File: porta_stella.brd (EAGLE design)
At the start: 220 x 100 mm, 85 parts, among them IC1 74LS00D, T1 2N3904, T2 PN3906, T3 PN3906, T4 PN3906, X1 SSW-112-02-G-Q

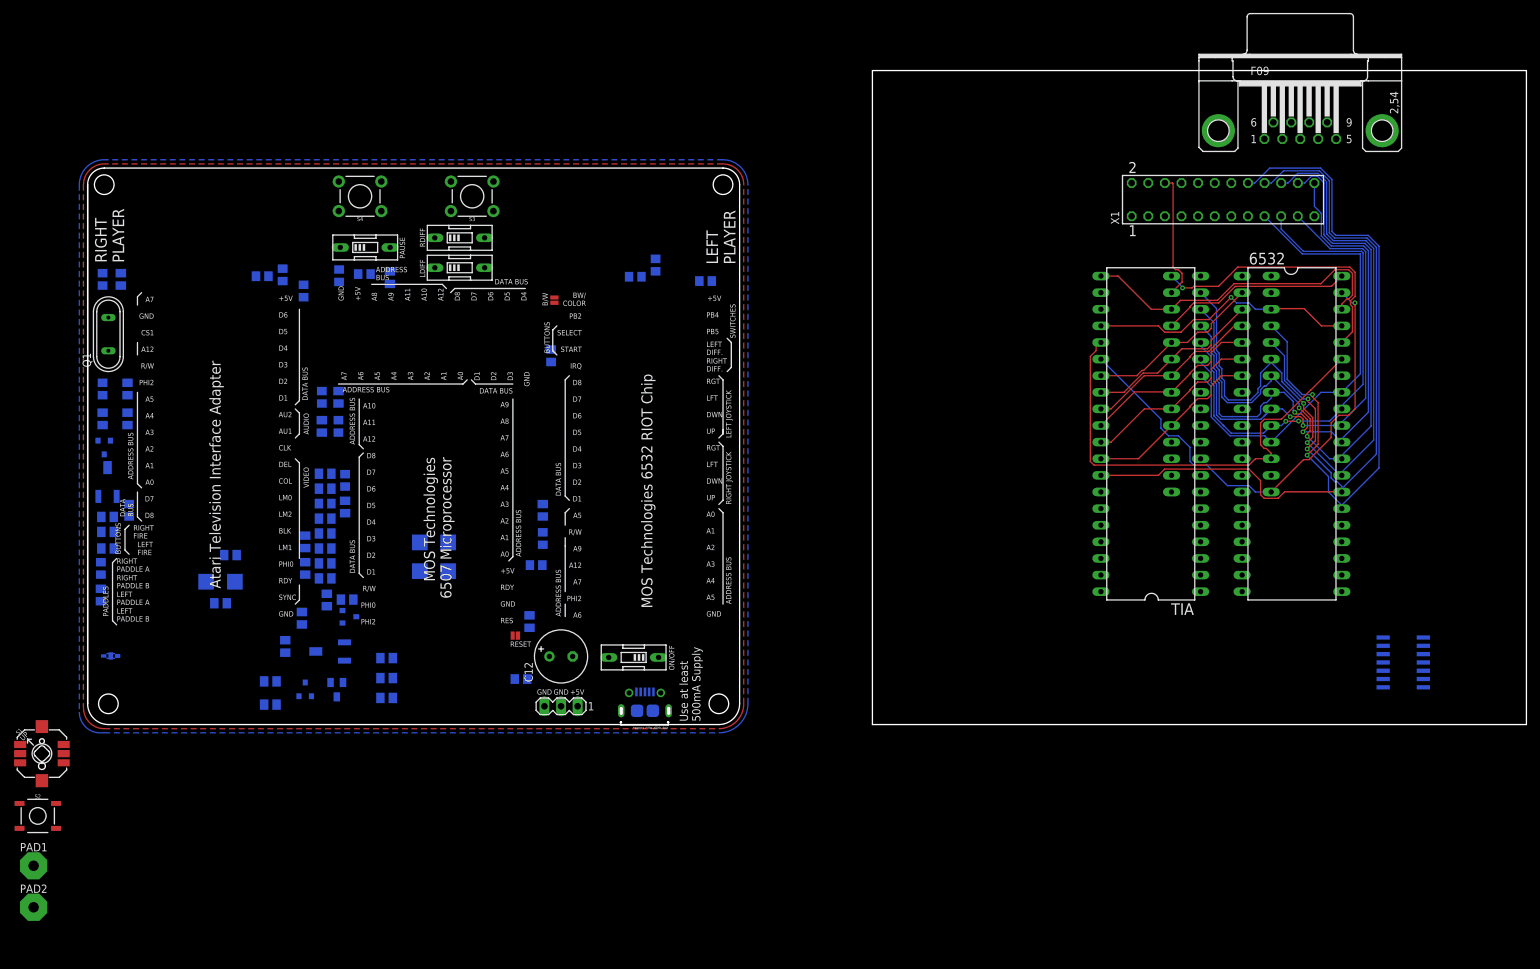
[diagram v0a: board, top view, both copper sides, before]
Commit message: more layout work for handheld
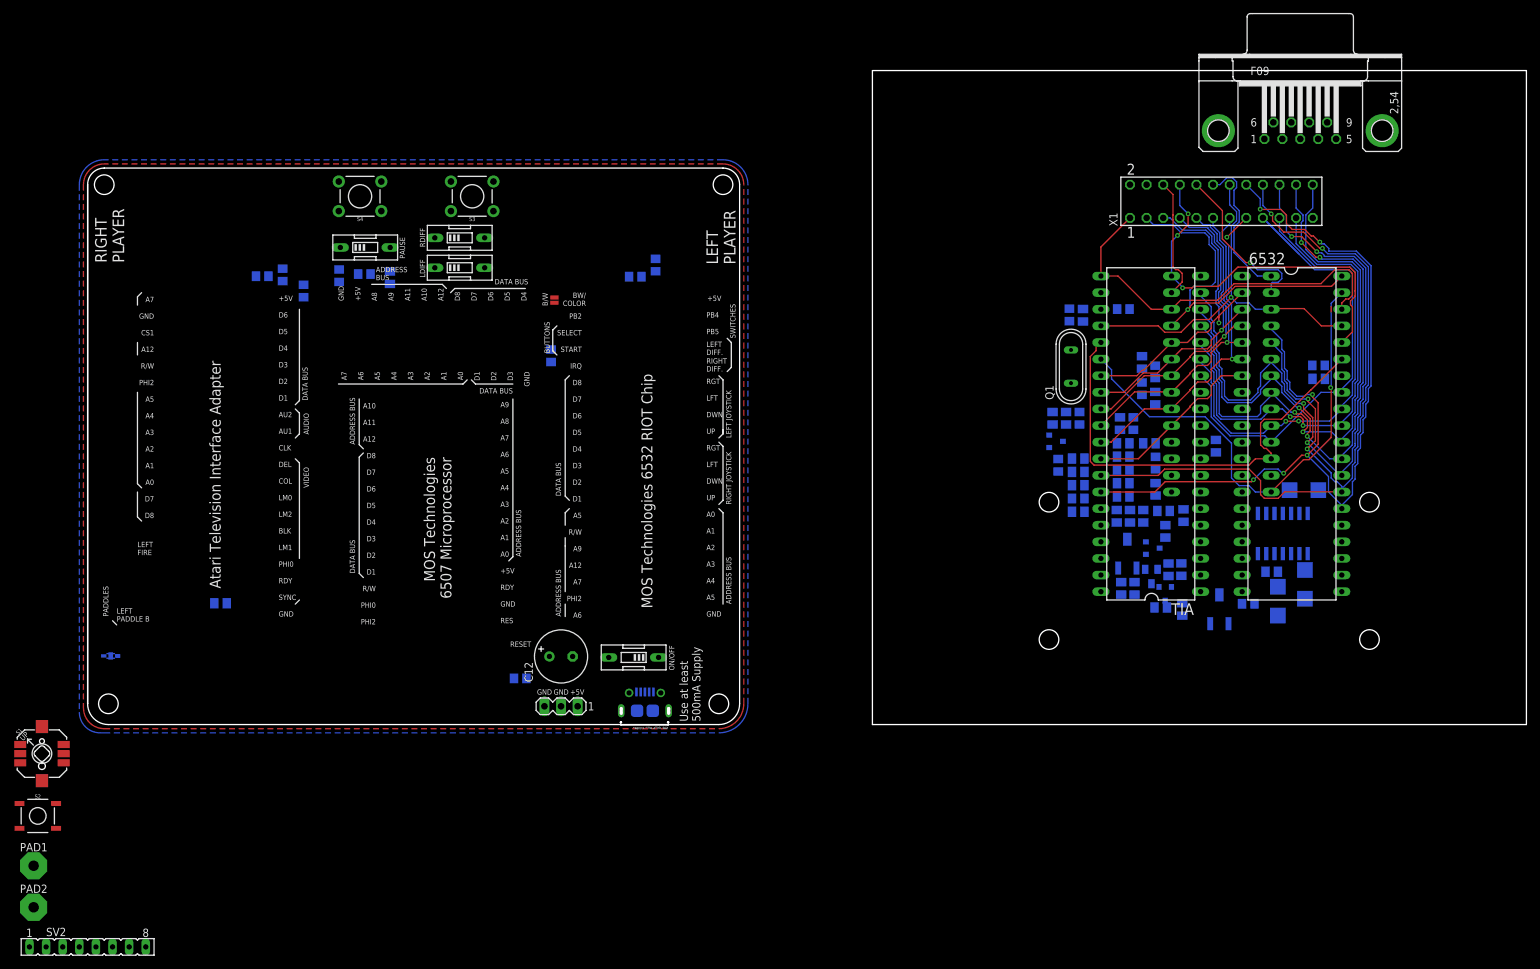
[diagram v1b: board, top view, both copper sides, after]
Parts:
- removed JP2: CPU_RES, SparkFun-Jumpers:SMT-JUMPER_2_NO_NO-SILK
- added SV2: (no value), con-lsta:FE08
- moved COLOR 171.1 mm to (173.1, 17.6)
- moved R31 166.5 mm to (172.5, 42.6), turned to 90 degrees
- moved D2 161.7 mm to (182.0, 18.9), turned to 90 degrees
- moved R32 159.2 mm to (181.1, 23.4)
- moved R15 150.4 mm to (151.5, 36.6), turned to 180 degrees
- moved C4 149.8 mm to (151.5, 34.6), turned to 180 degrees
- moved C19 149.4 mm to (151.7, 46.8), turned to 270 degrees
- moved R13 148.8 mm to (151.5, 40.7), turned to 0 degrees
- moved R14 148.6 mm to (151.5, 38.6)
- moved R16 148.5 mm to (151.5, 32.5)
- moved C20 147.9 mm to (150.1, 62.6)
- moved R29 147.3 mm to (149.6, 46.8)
- moved Q1 147.3 mm to (150.4, 54.7)
- moved R28 147.2 mm to (152.2, 62.6)
- moved T3 145.5 mm to (148.0, 43.3), turned to 90 degrees
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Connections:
- new net N$37: SV2.8
- new net N$41: SV2.7
- net GND: no longer JP2.2
- net N$23: no longer JP2.1
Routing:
- net D8: track 107.8 -> 134.6 mm, vias 2 -> 6
- net A6: track 29.3 -> 54.8 mm, vias 0 -> 1
- net A11: track 0.00 -> 25.4 mm, vias 0 -> 1
- net A5: track 27.3 -> 50.9 mm, vias 0 -> 1
- net A10: track 0.00 -> 23.1 mm
- net A1: track 27.7 -> 50.7 mm, vias 0 -> 1
- net A4: track 27.3 -> 49.3 mm, vias 0 -> 1
- net A3: track 26.9 -> 48.0 mm, vias 0 -> 1
- net A2: track 27.8 -> 48.2 mm, vias 0 -> 1
- net A12: track 41.3 -> 59.4 mm
- net A9: track 42.4 -> 57.9 mm, vias 1 -> 3
- net A7: track 49.6 -> 60.4 mm
- net D7: track 136.8 -> 129.7 mm, vias 2 -> 4
- net D6: track 113.1 -> 107.8 mm, vias 2 -> 4
- net D1: track 71.1 -> 75.6 mm
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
